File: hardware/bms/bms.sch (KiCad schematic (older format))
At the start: 198 parts, among them J1 Conn_01x08, J10 Conn_01x02, J11 Conn_01x02, J12 Conn_01x02, J13 Conn_01x10, J14 Conn_01x02, J15 Conn_01x02, J16 Cell Bypass, J2 Conn_01x04, J3 USB_B_Micro, J4 Conn_01x05, J5 Conn_01x04, J6 Conn_01x04, J7 Conn_01x03, J8 Conn_01x03, J9 Conn_01x02, M1 MountingHole, M2 MountingHole, M3 MountingHole, M4 MountingHole, M5 MountingHole, M6 MountingHole, Q1 BC817, Q10 ZXMP4A16G, Q11 IRF540N, Q12 IRF540N, Q13 BSS138, Q14 IRF540N, Q15 BSS138, Q16 BSS138, Q2 ZXMP4A16G, Q3 BSS138, Q4 BS170, Q5 IRF9540N, Q6 BC847, Q7 IRF9540N, Q8 BSS138, Q9 ZXMP4A16G, SW1 SW_DIP_x03, U1 USBLC6-2SC6, U2 STM32F042C6Tx, U3 TPS560430x3F, U4 TCAN334, U5 MAX485E, U6 LM5164DDAR, U7 LSI94202, Y1 8MHz

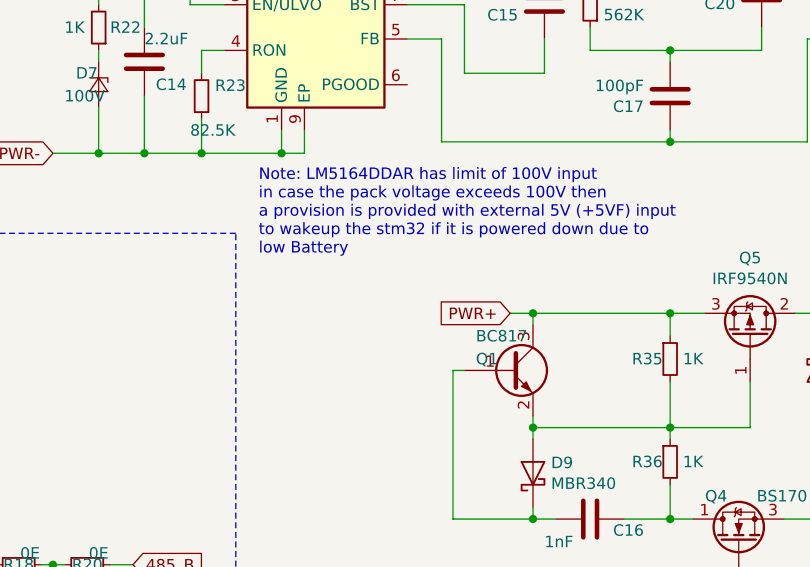
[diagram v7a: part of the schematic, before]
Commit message: added link to isolate charging power
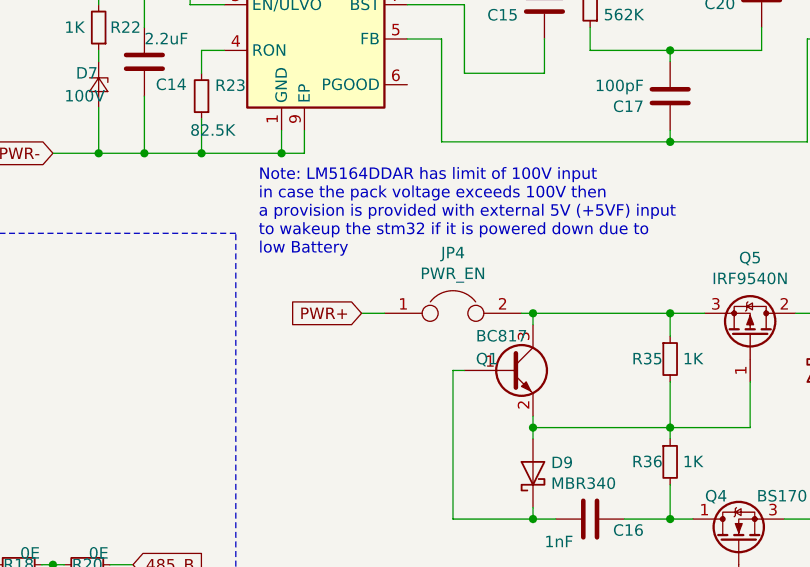
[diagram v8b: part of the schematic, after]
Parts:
- added JP4: PWR_EN, Connector_PinHeader_2.54mm:PinHeader_1x02_P2.54mm_Vertical, symbol BMS:JUMPER
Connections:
- net PWR+: now also JP4.1; no longer Q1.3 (C), Q5.3 (S), R35.1
- new net: JP4.2, Q1.3 (C), Q5.3 (S), R35.1
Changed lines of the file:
@@
 Text GLabel 9550 9050 0    50   Input ~ 0
 PWM
-Text GLabel 8700 7800 0    50   Input ~ 0
+Text GLabel 8050 7800 0    50   Input ~ 0
 PWR+
-Wire Wire Line
-	8700 7800 8800 7800
-Connection ~ 8800 7800
 Text GLabel 11100 7400 0    50   Input ~ 0
 PWR_OUT
@@
 	1    0    0    -1
 $EndComp
+$Comp
+L BMS:JUMPER JP4
+U 1 1 5E65E9A2
+P 8450 7800
+F 0 "JP4" H 8450 8064 50  0000 C CNN
+F 1 "PWR_EN" H 8450 7973 50  0000 C CNN
+F 2 "Connector_PinHeader_2.54mm:PinHeader_1x02_P2.54mm_Vertical" H 8450 7800 50  0001 C CNN
+F 3 "" H 8450 7800 50  0000 C CNN
+	1    8450 7800
+	1    0    0    -1
+$EndComp
+Wire Wire Line
+	8050 7800 8150 7800
+Wire Wire Line
+	8750 7800 8800 7800
+Connection ~ 8800 7800
 $EndSCHEMATC
